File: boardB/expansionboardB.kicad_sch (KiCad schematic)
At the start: 52 parts, among them J2 2086581051, J3 12402012E212A, SW1 ESPRST, SW4 ESPPROG, U1 ESP32-S3-WROOM-1, U2 GPIO_U2, U4 GPIO_U4, U5 SII1136CTU, U7 MAX20022ATIA+T, t1V2 1V2_TEST, t3V3 3V3_TEST, t5V2 5V_IN_TEST

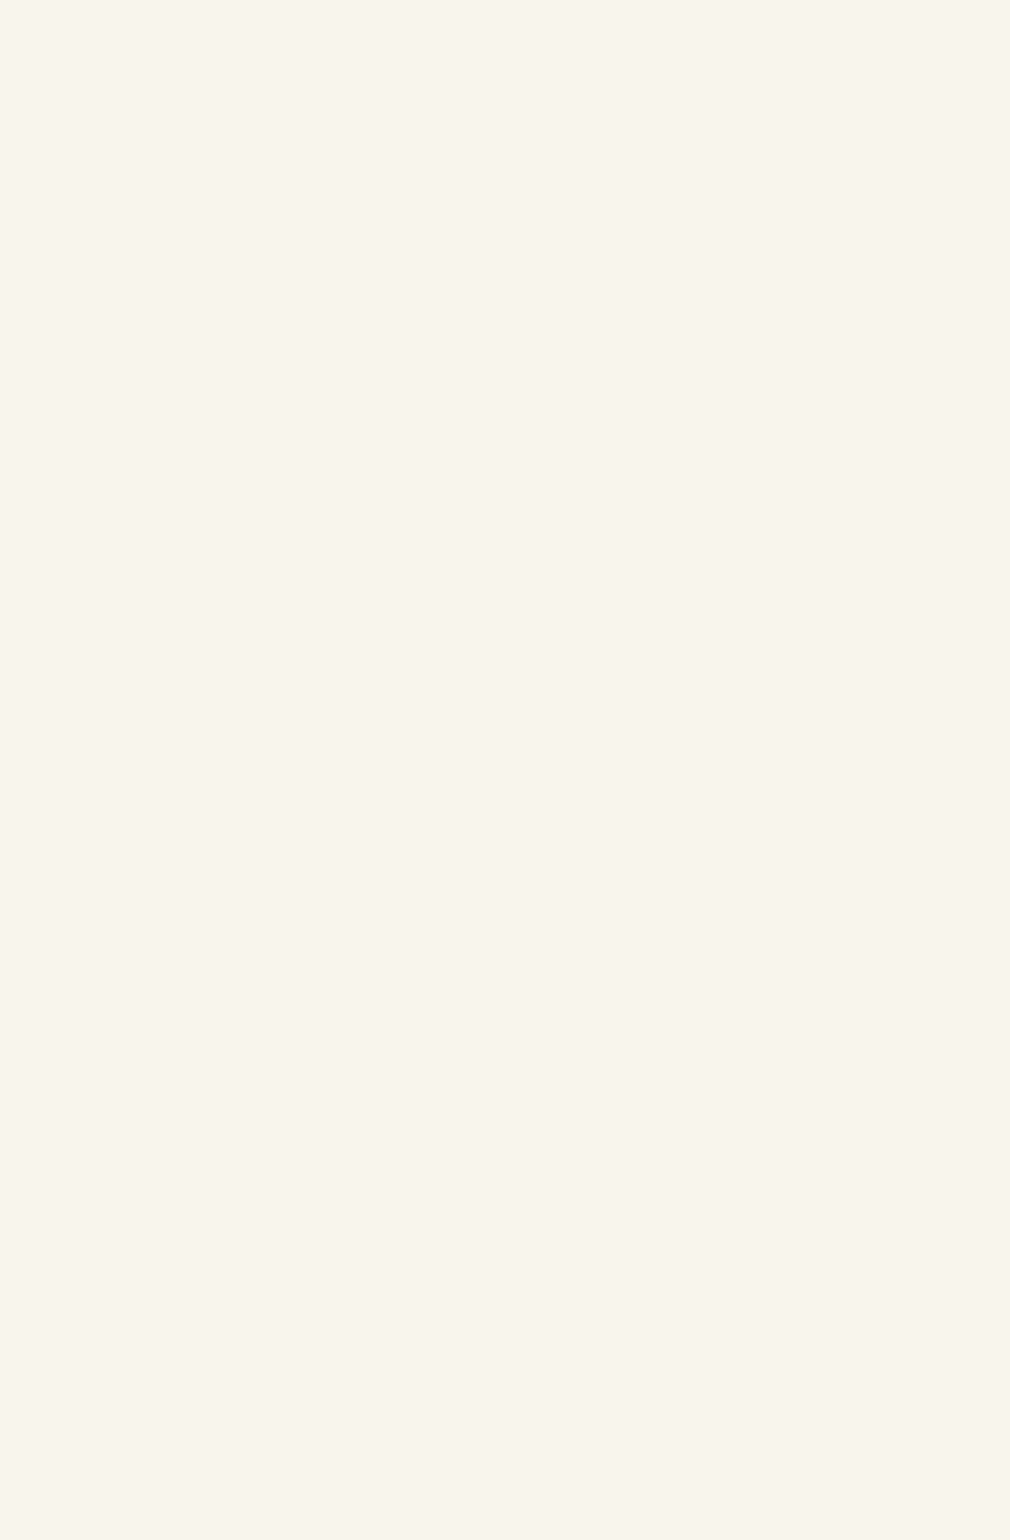
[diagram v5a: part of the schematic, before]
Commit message: Software can't cope with out-of-range devices, simply return 0
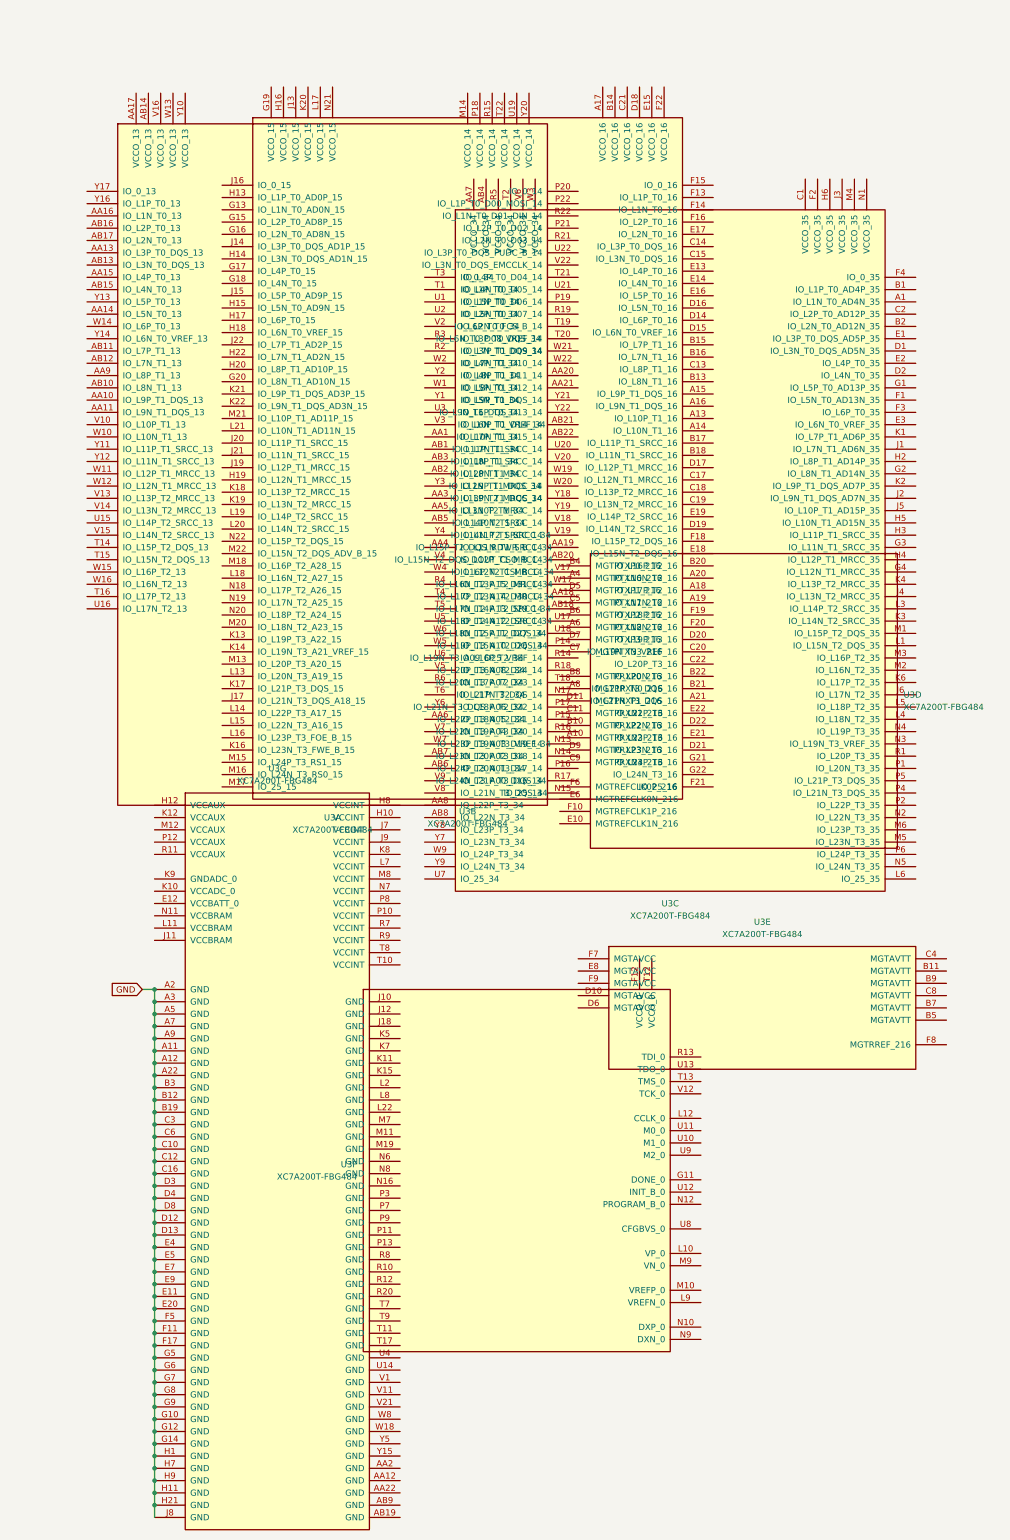
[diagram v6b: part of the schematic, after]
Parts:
- added U3: XC7A200T-FBG484, Package_BGA:Xilinx_FGG484, symbol FPGA_Xilinx_Artix7:XC7A200T-FBG484
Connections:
- net GND: now also U3.A11 (GND), U3.A12 (GND), U3.A2 (GND), U3.A22 (GND), U3.A3 (GND), U3.A5 (GND), U3.A7 (GND), U3.A9 (GND), U3.B12 (GND), U3.B19 (GND), U3.B3 (GND), U3.C10 (GND), U3.C12 (GND), U3.C16 (GND), U3.C3 (GND), U3.C6 (GND), U3.D12 (GND), U3.D13 (GND), U3.D3 (GND), U3.D4 (GND), U3.D8 (GND), U3.E11 (GND), U3.E20 (GND), U3.E4 (GND), U3.E5 (GND), U3.E7 (GND), U3.E9 (GND), U3.F11 (GND), U3.F17 (GND), U3.F5 (GND), U3.G10 (GND), U3.G12 (GND), U3.G14 (GND), U3.G5 (GND), U3.G6 (GND), U3.G7 (GND), U3.G8 (GND), U3.G9 (GND), U3.H1 (GND), U3.H11 (GND), U3.H21 (GND), U3.H7 (GND), U3.H9 (GND), U3.J8 (GND)
